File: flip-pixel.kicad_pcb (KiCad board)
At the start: 2 copper layers, 153 parts, among them Q1 DMN62D0U-7, Q10 STS8DN6LF6AG, Q13 STS8DN6LF6AG, Q16 STS8DN6LF6AG, Q19 STS8DN6LF6AG, Q22 STS8DN6LF6AG, Q25 STS8DN6LF6AG, Q28 STS8DN6LF6AG, Q29 DMN62D0U-7, Q30 DMN62D0U-7, Q31 STS8DN6LF6AG, Q4 STS8DN6LF6AG, Q7 STS8DN6LF6AG, U1 LM2665M6

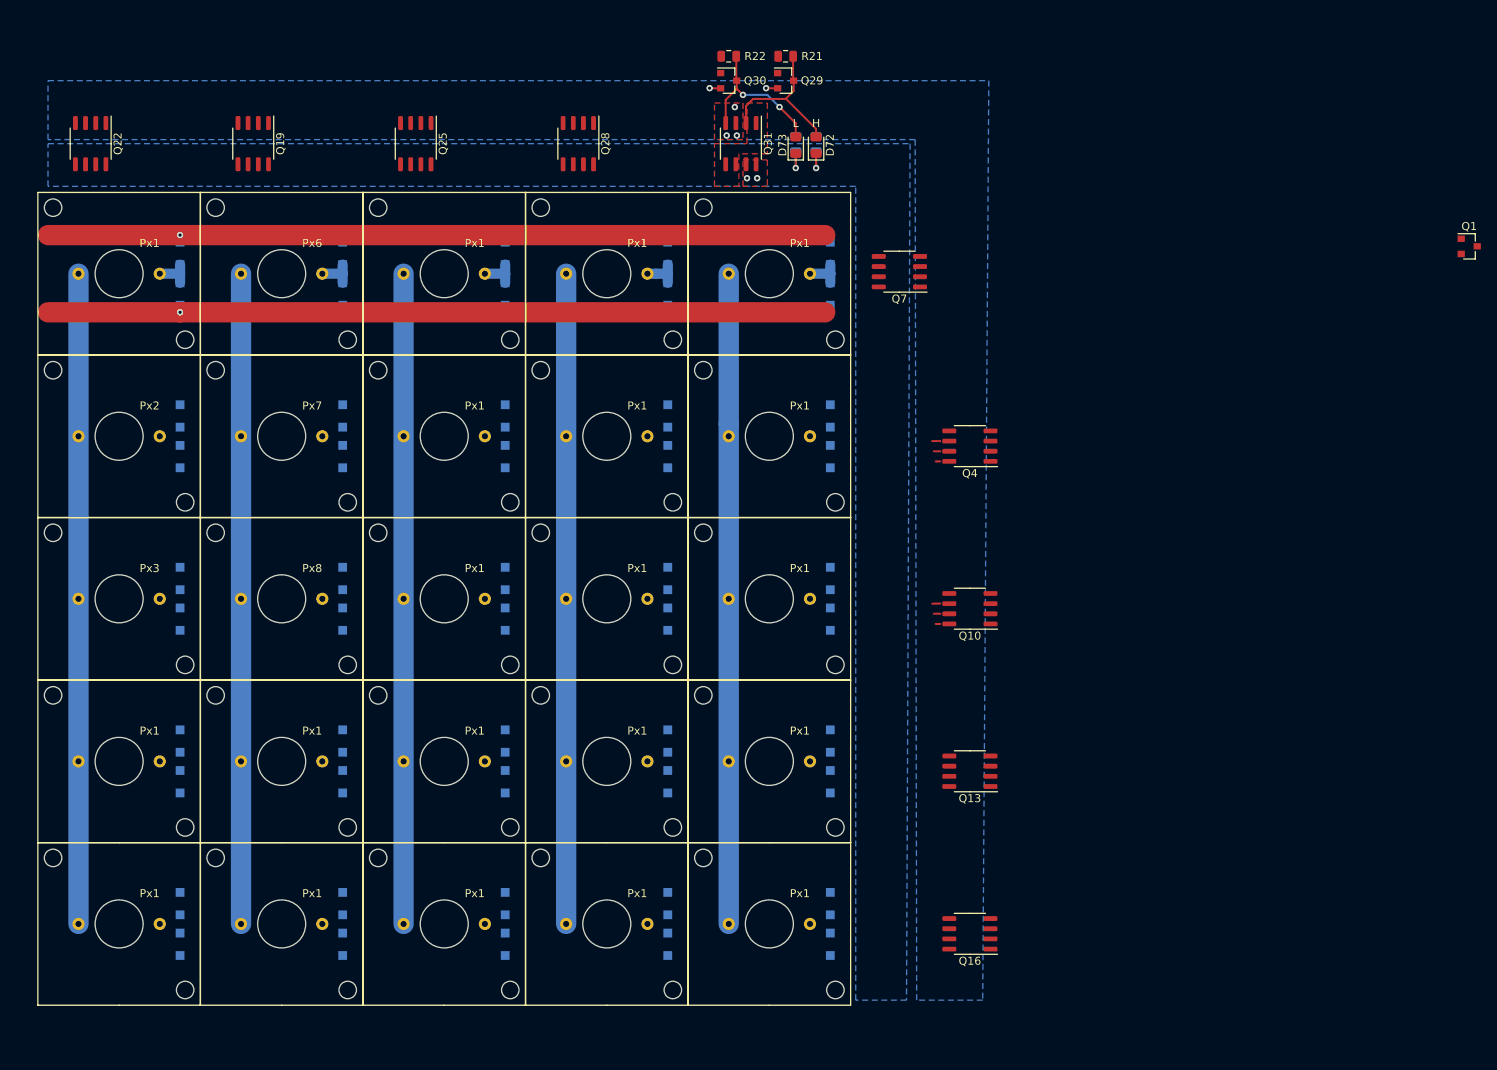
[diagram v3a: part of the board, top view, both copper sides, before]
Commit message: Replicated driving layout to all rows / columns
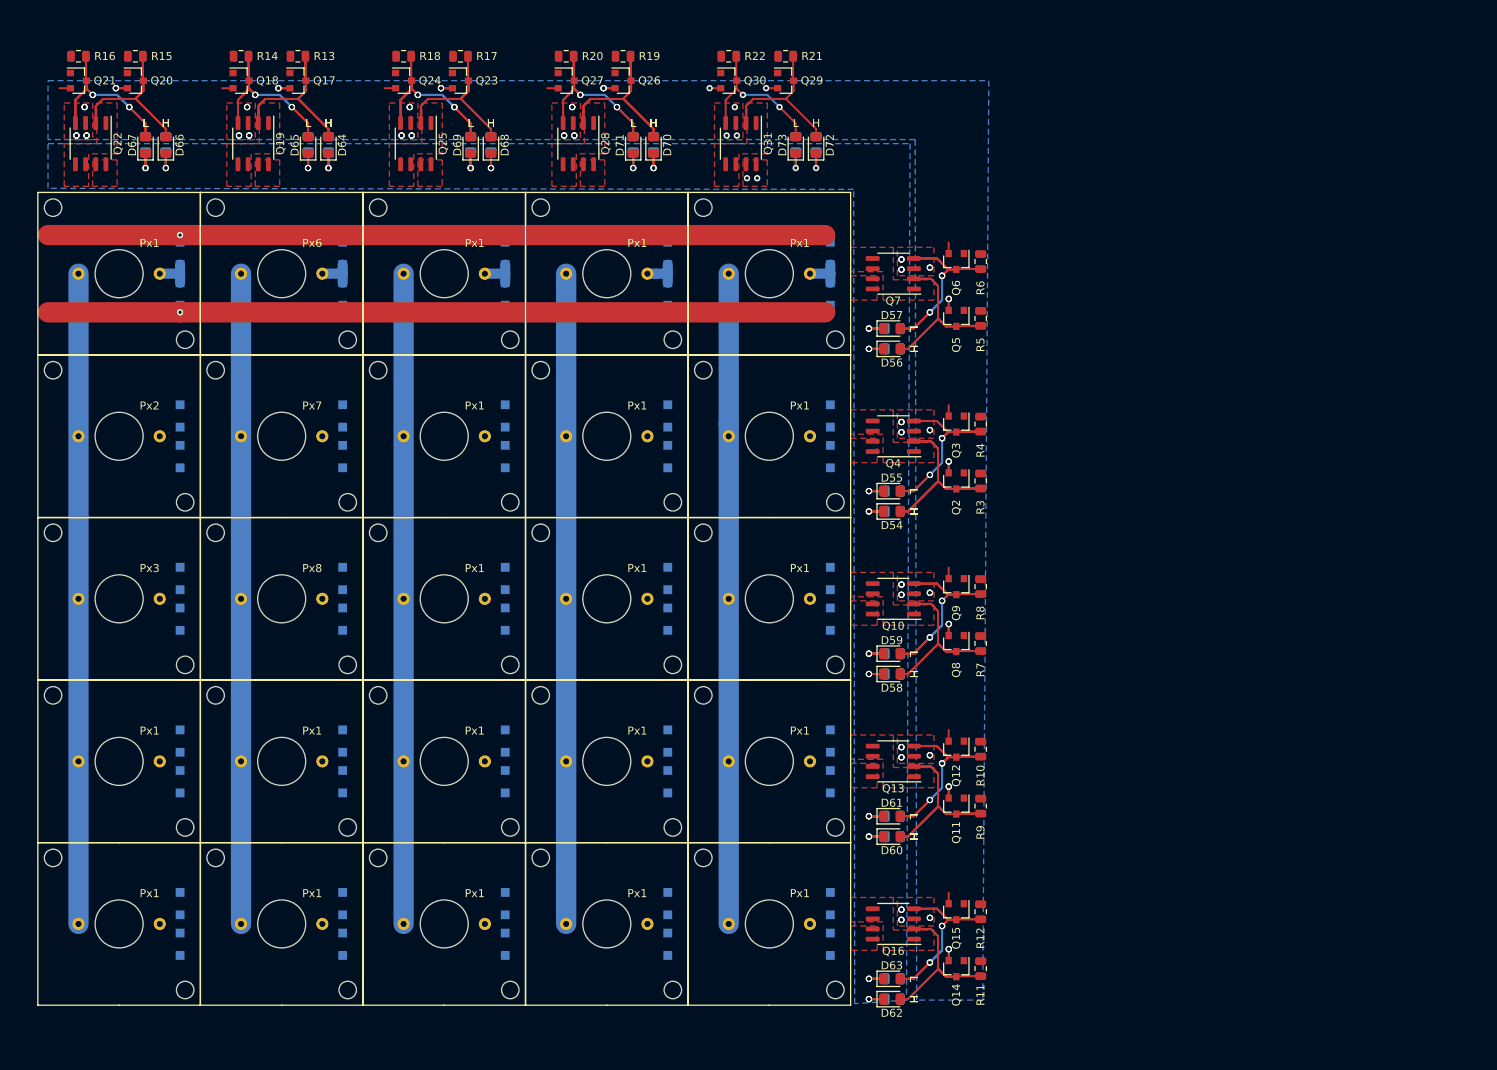
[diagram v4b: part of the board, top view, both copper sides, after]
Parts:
- removed Q1: DMN62D0U-7, Package_TO_SOT_SMD:SOT-23
- added D54: LED_Green, LED_SMD:LED_0805_2012Metric_Pad1.15x1.40mm_HandSolder, F.Cu at (264.2, 81.8)
- added D55: LED_Green, LED_SMD:LED_0805_2012Metric_Pad1.15x1.40mm_HandSolder, F.Cu at (264.2, 79.2)
- added D56: LED_Green, LED_SMD:LED_0805_2012Metric_Pad1.15x1.40mm_HandSolder, F.Cu at (264.2, 61.5)
- added D57: LED_Green, LED_SMD:LED_0805_2012Metric_Pad1.15x1.40mm_HandSolder, F.Cu at (264.2, 58.9)
- added D58: LED_Green, LED_SMD:LED_0805_2012Metric_Pad1.15x1.40mm_HandSolder, F.Cu at (264.2, 102.1)
- added D59: LED_Green, LED_SMD:LED_0805_2012Metric_Pad1.15x1.40mm_HandSolder, F.Cu at (264.2, 99.6)
- added D60: LED_Green, LED_SMD:LED_0805_2012Metric_Pad1.15x1.40mm_HandSolder, F.Cu at (264.2, 122.4)
- added D61: LED_Green, LED_SMD:LED_0805_2012Metric_Pad1.15x1.40mm_HandSolder, F.Cu at (264.2, 119.9)
- added D62: LED_Green, LED_SMD:LED_0805_2012Metric_Pad1.15x1.40mm_HandSolder, F.Cu at (264.2, 142.7)
- added D63: LED_Green, LED_SMD:LED_0805_2012Metric_Pad1.15x1.40mm_HandSolder, F.Cu at (264.2, 140.2)
- added D64: LED_Green, LED_SMD:LED_0805_2012Metric_Pad1.15x1.40mm_HandSolder, F.Cu at (193.8, 36.0)
- added D65: LED_Green, LED_SMD:LED_0805_2012Metric_Pad1.15x1.40mm_HandSolder, F.Cu at (191.3, 36.0)
- added D66: LED_Green, LED_SMD:LED_0805_2012Metric_Pad1.15x1.40mm_HandSolder, F.Cu at (173.5, 36.0)
- added D67: LED_Green, LED_SMD:LED_0805_2012Metric_Pad1.15x1.40mm_HandSolder, F.Cu at (170.9, 36.0)
- added D68: LED_Green, LED_SMD:LED_0805_2012Metric_Pad1.15x1.40mm_HandSolder, F.Cu at (214.1, 36.0)
- added D69: LED_Green, LED_SMD:LED_0805_2012Metric_Pad1.15x1.40mm_HandSolder, F.Cu at (211.6, 36.0)
- added D70: LED_Green, LED_SMD:LED_0805_2012Metric_Pad1.15x1.40mm_HandSolder, F.Cu at (234.4, 36.0)
- added D71: LED_Green, LED_SMD:LED_0805_2012Metric_Pad1.15x1.40mm_HandSolder, F.Cu at (231.9, 36.0)
- added Q11: DMN62D0U-7, Package_TO_SOT_SMD:SOT-23, F.Cu at (272.3, 118.6)
- added Q12: DMN62D0U-7, Package_TO_SOT_SMD:SOT-23, F.Cu at (272.3, 111.5)
- added Q14: DMN62D0U-7, Package_TO_SOT_SMD:SOT-23, F.Cu at (272.3, 138.9)
- added Q15: DMN62D0U-7, Package_TO_SOT_SMD:SOT-23, F.Cu at (272.3, 131.8)
- added Q17: DMN62D0U-7, Package_TO_SOT_SMD:SOT-23, F.Cu at (190.0, 27.9)
- added Q18: DMN62D0U-7, Package_TO_SOT_SMD:SOT-23, F.Cu at (182.9, 27.9)
- added Q2: DMN62D0U-7, Package_TO_SOT_SMD:SOT-23, F.Cu at (272.3, 78.0)
- added Q20: DMN62D0U-7, Package_TO_SOT_SMD:SOT-23, F.Cu at (169.7, 27.9)
- added Q21: DMN62D0U-7, Package_TO_SOT_SMD:SOT-23, F.Cu at (162.6, 27.9)
- added Q23: DMN62D0U-7, Package_TO_SOT_SMD:SOT-23, F.Cu at (210.3, 27.9)
- added Q24: DMN62D0U-7, Package_TO_SOT_SMD:SOT-23, F.Cu at (203.2, 27.9)
- added Q26: DMN62D0U-7, Package_TO_SOT_SMD:SOT-23, F.Cu at (230.6, 27.9)
- added Q27: DMN62D0U-7, Package_TO_SOT_SMD:SOT-23, F.Cu at (223.5, 27.9)
- added Q3: DMN62D0U-7, Package_TO_SOT_SMD:SOT-23, F.Cu at (272.3, 70.9)
- added Q5: DMN62D0U-7, Package_TO_SOT_SMD:SOT-23, F.Cu at (272.3, 57.7)
- added Q6: DMN62D0U-7, Package_TO_SOT_SMD:SOT-23, F.Cu at (272.3, 50.5)
- added Q8: DMN62D0U-7, Package_TO_SOT_SMD:SOT-23, F.Cu at (272.3, 98.3)
- added Q9: DMN62D0U-7, Package_TO_SOT_SMD:SOT-23, F.Cu at (272.3, 91.2)
- added R10: R, Resistor_SMD:R_0805_2012Metric, F.Cu at (275.3, 111.5)
- added R11: R, Resistor_SMD:R_0805_2012Metric, F.Cu at (275.3, 138.9)
- added R12: R, Resistor_SMD:R_0805_2012Metric, F.Cu at (275.3, 131.8)
- added R13: R, Resistor_SMD:R_0805_2012Metric, F.Cu at (190.0, 24.9)
- added R14: R, Resistor_SMD:R_0805_2012Metric, F.Cu at (182.9, 24.9)
- added R15: R, Resistor_SMD:R_0805_2012Metric, F.Cu at (169.7, 24.9)
- added R16: R, Resistor_SMD:R_0805_2012Metric, F.Cu at (162.6, 24.9)
- added R17: R, Resistor_SMD:R_0805_2012Metric, F.Cu at (210.3, 24.9)
- added R18: R, Resistor_SMD:R_0805_2012Metric, F.Cu at (203.2, 24.9)
- added R19: R, Resistor_SMD:R_0805_2012Metric, F.Cu at (230.6, 24.9)
- added R20: R, Resistor_SMD:R_0805_2012Metric, F.Cu at (223.5, 24.9)
- added R25: R, Resistor_SMD:R_0805_2012Metric, B.Cu at (264.4, 81.8)
- added R26: R, Resistor_SMD:R_0805_2012Metric, B.Cu at (264.4, 79.2)
- added R27: R, Resistor_SMD:R_0805_2012Metric, B.Cu at (264.4, 61.5)
- added R28: R, Resistor_SMD:R_0805_2012Metric, B.Cu at (264.4, 58.9)
- added R29: R, Resistor_SMD:R_0805_2012Metric, B.Cu at (264.4, 102.1)
- added R3: R, Resistor_SMD:R_0805_2012Metric, F.Cu at (275.3, 78.0)
- added R30: R, Resistor_SMD:R_0805_2012Metric, B.Cu at (264.4, 99.6)
- added R31: R, Resistor_SMD:R_0805_2012Metric, B.Cu at (264.4, 122.4)
- added R32: R, Resistor_SMD:R_0805_2012Metric, B.Cu at (264.4, 119.9)
- added R33: R, Resistor_SMD:R_0805_2012Metric, B.Cu at (264.4, 142.7)
- added R34: R, Resistor_SMD:R_0805_2012Metric, B.Cu at (264.4, 140.2)
- added R35: R, Resistor_SMD:R_0805_2012Metric, B.Cu at (193.8, 35.8)
- added R36: R, Resistor_SMD:R_0805_2012Metric, B.Cu at (191.3, 35.8)
- added R37: R, Resistor_SMD:R_0805_2012Metric, B.Cu at (173.5, 35.8)
- added R38: R, Resistor_SMD:R_0805_2012Metric, B.Cu at (170.9, 35.8)
- added R39: R, Resistor_SMD:R_0805_2012Metric, B.Cu at (214.1, 35.8)
- added R4: R, Resistor_SMD:R_0805_2012Metric, F.Cu at (275.3, 70.9)
- added R40: R, Resistor_SMD:R_0805_2012Metric, B.Cu at (211.6, 35.8)
- added R41: R, Resistor_SMD:R_0805_2012Metric, B.Cu at (234.4, 35.8)
- added R42: R, Resistor_SMD:R_0805_2012Metric, B.Cu at (231.9, 35.8)
- added R5: R, Resistor_SMD:R_0805_2012Metric, F.Cu at (275.3, 57.7)
- added R6: R, Resistor_SMD:R_0805_2012Metric, F.Cu at (275.3, 50.5)
- added R7: R, Resistor_SMD:R_0805_2012Metric, F.Cu at (275.3, 98.3)
- added R8: R, Resistor_SMD:R_0805_2012Metric, F.Cu at (275.3, 91.2)
- added R9: R, Resistor_SMD:R_0805_2012Metric, F.Cu at (275.3, 118.6)
- moved Q10 9.66 mm to (264.4, 92.7)
- moved Q13 9.66 mm to (264.4, 113.0)
- moved Q16 9.66 mm to (264.4, 133.3)
- moved Q4 9.66 mm to (264.4, 72.4)
- moved Q7 0.80 mm to (264.4, 52.1)
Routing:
- net /Row4/Gate_L: track 0.00 -> 40.1 mm, vias 0 -> 4
- net /Row2/Gate_L: track 0.00 -> 40.1 mm, vias 0 -> 4
- net /Row1/Gate_L: track 0.00 -> 40.1 mm, vias 0 -> 4
- net /Row5/Gate_L: track 0.00 -> 40.1 mm, vias 0 -> 4
- net /Row3/Gate_L: track 0.00 -> 40.1 mm, vias 0 -> 4
- net /Column2/Gate_L: track 0.00 -> 40.1 mm, vias 0 -> 4
- net /Column1/Gate_L: track 0.00 -> 40.1 mm, vias 0 -> 4
- net /Column3/Gate_L: track 0.00 -> 40.1 mm, vias 0 -> 4
- net /Column4/Gate_L: track 0.00 -> 40.1 mm, vias 0 -> 4
- net /Row3/Gate_H: track 0.00 -> 39.8 mm
- net /Row1/Gate_H: track 0.00 -> 39.8 mm
- net /Row4/Gate_H: track 0.00 -> 39.8 mm
- net /Row2/Gate_H: track 0.00 -> 39.8 mm
- net /Row5/Gate_H: track 0.00 -> 39.8 mm
- net /Column2/Gate_H: track 0.00 -> 39.8 mm
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- added copper zone on F.Cu, net /PixelMatrix/Col_1
- added copper zone on F.Cu, net /PixelMatrix/Col_2
- added copper zone on F.Cu, net /PixelMatrix/Col_3
- added copper zone on F.Cu, net /PixelMatrix/Col_4
- added copper zone on F.Cu, net /Row1/High
- added copper zone on F.Cu, net /Row2/High
- added copper zone on F.Cu, net /Row3/High
- added copper zone on F.Cu, net /Row4/High
- added copper zone on F.Cu, net /Row5/High

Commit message: Updated references for pixels
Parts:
- added Q1: DMN62D0U-7, Package_TO_SOT_SMD:SOT-23, F.Cu at (121.7, 21.6)
- renumbered Px1 to Px10, Px1 to Px11, Px1 to Px12, Px1 to Px13, Px1 to Px14, Px1 to Px15, Px1 to Px16, Px1 to Px17, Px1 to Px18, Px1 to Px19, Px1 to Px20, Px1 to Px21, Px1 to Px22, Px1 to Px23, Px1 to Px24, Px1 to Px25, Px1 to Px4, Px1 to Px5, Px1 to Px9
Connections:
- Px10 pad 1: Net-(D2-Pad1) -> Net-(D20-Pad1)
- Px10 pad 2: /PixelMatrix/Col_1 -> /PixelMatrix/Col_2
- Px11 pad 1: Net-(D2-Pad1) -> Net-(D22-Pad1)
- Px11 pad 2: /PixelMatrix/Col_1 -> /PixelMatrix/Col_3
- Px12 pad 1: Net-(D2-Pad1) -> Net-(D24-Pad1)
- Px12 pad 2: /PixelMatrix/Col_1 -> /PixelMatrix/Col_3
- Px13 pad 1: Net-(D2-Pad1) -> Net-(D26-Pad1)
- Px13 pad 2: /PixelMatrix/Col_1 -> /PixelMatrix/Col_3
- Px14 pad 1: Net-(D2-Pad1) -> Net-(D28-Pad1)
- Px14 pad 2: /PixelMatrix/Col_1 -> /PixelMatrix/Col_3
- Px15 pad 1: Net-(D2-Pad1) -> Net-(D30-Pad1)
- Px15 pad 2: /PixelMatrix/Col_1 -> /PixelMatrix/Col_3
- Px16 pad 1: Net-(D2-Pad1) -> Net-(D32-Pad1)
- Px16 pad 2: /PixelMatrix/Col_1 -> /PixelMatrix/Col_4
- Px17 pad 1: Net-(D2-Pad1) -> Net-(D34-Pad1)
- Px17 pad 2: /PixelMatrix/Col_1 -> /PixelMatrix/Col_4
- Px18 pad 1: Net-(D2-Pad1) -> Net-(D36-Pad1)
- Px18 pad 2: /PixelMatrix/Col_1 -> /PixelMatrix/Col_4
- Px19 pad 1: Net-(D2-Pad1) -> Net-(D38-Pad1)
- Px19 pad 2: /PixelMatrix/Col_1 -> /PixelMatrix/Col_4
- Px20 pad 1: Net-(D2-Pad1) -> Net-(D40-Pad1)
- Px20 pad 2: /PixelMatrix/Col_1 -> /PixelMatrix/Col_4
- Px21 pad 1: Net-(D2-Pad1) -> Net-(D42-Pad1)
- Px21 pad 2: /PixelMatrix/Col_1 -> /PixelMatrix/Col_5
- Px22 pad 1: Net-(D2-Pad1) -> Net-(D44-Pad1)
- Px22 pad 2: /PixelMatrix/Col_1 -> /PixelMatrix/Col_5
- Px23 pad 1: Net-(D2-Pad1) -> Net-(D46-Pad1)
- Px23 pad 2: /PixelMatrix/Col_1 -> /PixelMatrix/Col_5
- Px24 pad 1: Net-(D2-Pad1) -> Net-(D48-Pad1)
- Px24 pad 2: /PixelMatrix/Col_1 -> /PixelMatrix/Col_5
- Px25 pad 1: Net-(D2-Pad1) -> Net-(D50-Pad1)
- Px25 pad 2: /PixelMatrix/Col_1 -> /PixelMatrix/Col_5
- Px4 pad 1: Net-(D2-Pad1) -> Net-(D8-Pad1)
- Px5 pad 1: Net-(D2-Pad1) -> Net-(D10-Pad1)
- Px9 pad 1: Net-(D2-Pad1) -> Net-(D18-Pad1)
- Px9 pad 2: /PixelMatrix/Col_1 -> /PixelMatrix/Col_2
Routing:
- net /PixelMatrix/Col_1: track 406.4 -> 81.3 mm
- net /PixelMatrix/Col_5: track 0.00 -> 81.3 mm
- net /PixelMatrix/Col_4: track 0.00 -> 81.3 mm
- net /PixelMatrix/Col_3: track 0.00 -> 81.3 mm
- net /PixelMatrix/Col_2: track 0.00 -> 81.3 mm
- net GND: vias 57 -> 66
